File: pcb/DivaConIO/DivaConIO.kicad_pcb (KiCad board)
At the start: 2 copper layers, 65 x 75 mm, 59 parts, among them J1 Conn_01x06_MountingPin, J2 Conn_01x04_MountingPin, J3 Conn_01x06_MountingPin, J4 Conn_01x08_MountingPin, J5 JST_SH_BM03B-SRSS-TB, J6 Conn_01x05_MountingPin, J7 Conn_01x06_MountingPin, Q1 BSS138, Q2 BSS138, Q3 BSS138, Q4 BSS138, Q5 BSS138, SW1 SW_Push

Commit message: revision 1.0 pcb schematics and layout
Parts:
- removed C5, C6: 1u0, Capacitor_SMD:C_0603_1608Metric
- removed Q1: BSS138, Package_TO_SOT_SMD:SOT-23
- added C7: 100n, Capacitor_SMD:C_0603_1608Metric, F.Cu at (117.3, 124.9)
- added FID1: Fiducial, Fiducial:Fiducial_0.5mm_Mask1.5mm, F.Cu at (163.2, 142.0)
- added FID2: Fiducial, Fiducial:Fiducial_0.5mm_Mask1.5mm, F.Cu at (108.0, 76.8)
- added FID3: Fiducial, Fiducial:Fiducial_0.5mm_Mask1.5mm, F.Cu at (101.8, 83.0)
- added FID4: Fiducial, Fiducial:Fiducial_0.5mm_Mask1.5mm, F.Cu at (157.0, 148.2)
- added TP1: TestPoint, TestPoint:TestPoint_Pad_D2.0mm, F.Cu at (147.5, 87.8)
- added TP10: TestPoint, TestPoint:TestPoint_Pad_D2.0mm, F.Cu at (143.5, 135.5)
- added TP11: TestPoint, TestPoint:TestPoint_Pad_D2.0mm, F.Cu at (140.5, 142.8)
- added TP12: TestPoint, TestPoint:TestPoint_Pad_D2.0mm, F.Cu at (140.5, 138.7)
- added TP2: TestPoint, TestPoint:TestPoint_Pad_D2.0mm, F.Cu at (150.8, 79.2)
- added TP3: TestPoint, TestPoint:TestPoint_Pad_D2.0mm, F.Cu at (112.5, 135.5)
- added TP4: TestPoint, TestPoint:TestPoint_Pad_D2.0mm, F.Cu at (153.0, 82.5)
- added TP5: TestPoint, TestPoint:TestPoint_Pad_D2.0mm, F.Cu at (120.5, 133.0)
- added TP6: TestPoint, TestPoint:TestPoint_Pad_D2.0mm, F.Cu at (123.5, 133.0)
- added TP7: TestPoint, TestPoint:TestPoint_Pad_D2.0mm, F.Cu at (140.5, 130.0)
- added TP8: TestPoint, TestPoint:TestPoint_Pad_D2.0mm, F.Cu at (140.5, 133.0)
- added TP9: TestPoint, TestPoint:TestPoint_Pad_D2.0mm, F.Cu at (156.8, 112.5)
- added U1: 74HCT1G14, Package_TO_SOT_SMD:SC-74A-5_1.55x2.9mm_P0.95mm, F.Cu at (117.3, 121.8)
- J1, J3, J7: value Conn_01x06_MountingPin -> B6B-PH-SM4-TBT
- J2: value Conn_01x04_MountingPin -> B4B-PH-SM4-TBT
- J4: value Conn_01x08_MountingPin -> B8B-PH-SM4-TBT
- J5: value JST_SH_BM03B-SRSS-TB -> BM03B-SRSS-TBT
- R18: value 4K7 -> 330R
- R19: value 10R -> 10K
- SW1: footprint Button_Switch_SMD:SW_Push_SPST_NO_Alps_SKRK -> DivaConIO:SW_Push_SPST_NO_Alps_SKRP
- moved SYM2 37.6 mm to (129.0, 101.0)
- moved SYM1 37.5 mm to (136.0, 100.5)
- moved R16 24.3 mm to (146.5, 125.4), turned to 90 degrees
- moved R17 23.8 mm to (146.5, 122.3), turned to -90 degrees
- moved R9 23.7 mm to (117.3, 102.2), turned to 0 degrees
- moved R10 23.2 mm to (117.3, 104.8), turned to 0 degrees
- moved R32 20.3 mm to (147.2, 109.9), turned to 180 degrees
- moved R11 20.2 mm to (117.3, 109.9), turned to 0 degrees
- moved R31 19.8 mm to (147.2, 112.4), turned to 180 degrees
- moved R12 19.7 mm to (117.3, 112.4), turned to 0 degrees
- moved R30 19.3 mm to (147.2, 114.9), turned to 180 degrees
- moved R29 18.8 mm to (147.2, 117.5), turned to 180 degrees
- moved R14 18.7 mm to (117.3, 115.5), turned to 0 degrees
- moved R6 18.3 mm to (117.3, 92.3), turned to 0 degrees
- moved R18 16.8 mm to (114.7, 123.8), turned to -90 degrees
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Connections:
- net /LED_Circle renamed /LED-_Circle
- net /LED_Cross renamed /LED-_Cross
- net /LED_Square renamed /LED-_Square
- net /LED_Triangle renamed /LED-_Triangle
- J4 pad 4: Net-(J4-Pin_4) -> /Slider_I2C1_SDA
- J4 pad 6: /Slider_I2C1_SDA -> Net-(J4-Pin_6)
- J5 pad 1: Net-(A1-SWDIO) -> Net-(A1-SWCLK)
- J5 pad 3: Net-(A1-SWCLK) -> Net-(A1-SWDIO)
- R13 pad 2: /Slider_I2C1_SDA -> /Slider_I2C1_SCL
- R15 pad 2: /Slider_I2C1_SCL -> /Slider_I2C1_SDA
- R18 pad 1: +5V -> Net-(R18-Pad1)
- R18 pad 2: Net-(J4-Pin_4) -> Net-(J4-Pin_6)
- R19 pad 2: Net-(Q1-G) -> GND
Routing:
- net GND: track 123.4 -> 25.3 mm, vias 16 -> 512
- net +5V: track 139.6 -> 187.6 mm, vias 4 -> 25
- net +3V3: track 199.6 -> 245.4 mm, vias 24 -> 39
- net Net-(J4-Pin_6): track 0.00 -> 27.0 mm
- net /Slider_LED_Data: track 22.6 -> 7.62 mm
- net /Display_I2C0_SDA: track 33.3 -> 46.5 mm
- net Net-(J4-Pin_4): track 9.00 -> 0.00 mm
- net /Display_I2C0_SCL: track 40.7 -> 48.7 mm
- net Net-(A1-SWDIO): track 30.2 -> 36.7 mm, vias 0 -> 2
- net /LED-_Triangle: track 10.1 -> 16.5 mm
- net /Slider_I2C1_SCL: track 21.9 -> 27.8 mm
- net /Button_L1: track 32.2 -> 37.9 mm
- net /Button_R3: track 22.4 -> 27.9 mm
- net Net-(A1-SWCLK): track 31.5 -> 36.6 mm
- net /Button_Right: track 25.4 -> 30.4 mm
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- added copper zone on B.Cu, net +3V3
- added copper zone on F.Cu, net +3V3
- added copper zone on B.Cu, net +5V
- added copper zone on F.Cu, net +5V
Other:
- outline, holes or cut-outs redrawn
- board text added: "${TITLE} ${COMPANY} Rev ${REVISION} ${ISSUE_DATE}"
- board text added: "0.2032 mm / 0.2032 mm"
- board text added: "0.4000 mm"
- board text added: "1"
- board text added: "1.6000 mm"
- board text added: "2"
- board text added: "3V3"
- board text added: "5V"
- board text added: "65.0000 mm x 75.0000 mm"
- board text added: "BOARD CHARACTERISTICS"
- board text added: "Board Thickness:"
- board text added: "Board overall dimensions:"
- board text added: "Castellated pads:"
- board text added: "Copper Finish:"
- board text added: "Copper Layer Count:"
- board text added: "ENIG"
- board text added: "Edge card connectors:"
- board text added: "GND"
- board text added: "Impedance Control:"
- board text added: "LED_DATA"
- board text added: "Min hole diameter:"
- board text added: "Min track/spacing:"
- board text added: "No"
- board text added: "Plated Board Edge:"
- board text added: "RESET"
- board text added: "SCL0"
- board text added: "SCL1"
- board text added: "SDA0"
- board text added: "SDA1"
- board text added: "SN:"
- board text added: "SWCLK"
- board text added: "SWDIO"
- board text added: "nRST"

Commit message: revision 1.1 pcb schematics and layout
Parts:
- removed the R23 at (146.5, 95.8)
- removed the R26 at (152.2, 99.4)
- added R20: 10R, Resistor_SMD:R_0603_1608Metric, F.Cu at (147.2, 95.9)
- added R32: 330R, Resistor_SMD:R_0603_1608Metric, F.Cu at (153.3, 104.5)
- moved TP6 56.8 mm to (151.3, 83.5), turned to 0 degrees
- moved TP5 54.9 mm to (151.3, 87.5), turned to 0 degrees
- moved TP3 54.2 mm to (158.0, 106.0)
- moved TP2 53.1 mm to (135.0, 130.0)
- moved SYM1 51.2 mm to (106.0, 142.0)
- moved SYM2 47.8 mm to (145.0, 146.0)
- moved TP1 45.7 mm to (130.0, 130.0)
- moved J6 41.7 mm to (160.0, 128.0), turned to -90 degrees
- moved R31 35.4 mm to (149.0, 109.6), turned to -90 degrees
- moved TP11 34.9 mm to (151.3, 109.6), turned to 0 degrees
- moved R11 33.4 mm to (115.7, 123.4), turned to 90 degrees
- moved C5 31.6 mm to (148.1, 131.7)
- moved R23 31.5 mm to (148.1, 125.1), turned to 0 degrees
- moved U1 31.5 mm to (148.1, 128.4)
- moved R26 31.3 mm to (145.2, 130.9)
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- renumbered C7 to C5, FID3 to FID2, FID2 to FID3, J6 to J4, J4 to J6, Q5 to Q1, Q4 to Q2, Q2 to Q4, R9 to R10, R31 to R11, R10 to R12, R30 to R13, R11 to R14, R29 to R15, R12 to R16, R14 to R17, R20 to R18, R24 to R19, R19 to R23, R28 to R24, R18 to R26, R17 to R28, R16 to R29, R15 to R30, R13 to R31, R32 to R9
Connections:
- A1 pad 17: /Slider_LED_Data -> /Button_Circle
- A1 pad 19: /Slider_I2C1_SDA -> /Button_Cross
- A1 pad 20: /Slider_I2C1_SCL -> /Button_Square
- A1 pad 21: /Display_I2C0_SDA -> /Button_Triangle
- A1 pad 22: /Display_I2C0_SCL -> /Slider_LED_Data
- A1 pad 24: /Button_Triangle -> /Slider_I2C1_SDA
- A1 pad 25: /Button_Square -> /Slider_I2C1_SCL
- A1 pad 26: /Button_Cross -> /Display_I2C0_SDA
- A1 pad 27: /Button_Circle -> /Display_I2C0_SCL
- A1 pad 29: /LED_En_Triangle -> /LED_En_Circle
- A1 pad 31: /LED_En_Square -> /LED_En_Cross
- A1 pad 32: /LED_En_Cross -> /LED_En_Square
- A1 pad 34: /LED_En_Circle -> /LED_En_Triangle
- J4 pad 2: /Button_Circle -> /Button_Triangle
- J4 pad 3: /Button_Cross -> /Button_Square
- J4 pad 4: /Button_Square -> /Button_Cross
- J4 pad 5: /Button_Triangle -> /Button_Circle
- J6 pad 1: GND -> /Display_I2C0_SCL
- J6 pad 2: /Display_I2C0_SCL -> /Display_I2C0_SDA
- J6 pad 3: /Display_I2C0_SDA -> /Slider_I2C1_SCL
- J6 pad 5: /Slider_I2C1_SCL -> +3V3
- J6 pad 6: Net-(J4-Pin_6) -> GND
- J6 pad 7: +3V3 -> +5V
- J6 pad 8: +5V -> Net-(J6-Pin_8)
- J7 pad 1: /LED-_Circle -> +5V
- J7 pad 2: /LED-_Cross -> +5V
- J7 pad 3: /LED-_Square -> /LED-_Triangle
- J7 pad 4: /LED-_Triangle -> /LED-_Square
- J7 pad 5: +5V -> /LED-_Cross
- J7 pad 6: +5V -> /LED-_Circle
- Q2 pad 3: Net-(Q4-D) -> Net-(Q2-D)
- Q4 pad 1: Net-(Q2-G) (its old number) -> Net-(Q4-G)
- Q4 pad 3: Net-(Q2-D) -> Net-(Q4-D)
- R19 pad 1: /LED_En_Circle -> /LED_En_Triangle
- R21 pad 1: /LED_En_Triangle -> /LED_En_Cross
- R21 pad 2: Net-(Q2-G) (its old number) -> Net-(Q3-G)
- R22 pad 1: /LED_En_Square -> /LED_En_Circle
- R22 pad 2: Net-(Q3-G) -> Net-(Q4-G)
- R24 pad 1: /LED-_Circle -> /LED-_Triangle
- R25 pad 1: /LED-_Triangle -> /LED-_Square
- R26 pad 2: Net-(J4-Pin_6) -> Net-(J6-Pin_8)
- R27 pad 2: Net-(Q4-D) -> Net-(Q3-D)
- R28 pad 2: /Display_I2C0_SCL -> /Slider_I2C1_SDA
- R29 pad 2: /Display_I2C0_SDA -> /Slider_I2C1_SCL
- R30 pad 2: /Slider_I2C1_SDA -> /Display_I2C0_SDA
- R31 pad 2: /Slider_I2C1_SCL -> /Display_I2C0_SCL
- TP1 pad 1: +3V3 -> Net-(A1-SWCLK)
- TP10 pad 1: GND -> /Display_I2C0_SDA
- TP11 pad 1: Net-(A1-SWCLK) -> /Display_I2C0_SCL
- TP12 pad 1: Net-(A1-SWDIO) -> GND
- TP2 pad 1: +5V -> Net-(A1-SWDIO)
- TP3 pad 1: Net-(J4-Pin_6) -> Net-(A1-RUN)
- TP4 pad 1: GND -> +5V
- TP5 pad 1: /Slider_I2C1_SCL -> +3V3
- TP6 pad 1: /Slider_I2C1_SDA -> GND
- TP7 pad 1: /Display_I2C0_SDA -> Net-(J6-Pin_8)
- TP8 pad 1: /Display_I2C0_SCL -> /Slider_I2C1_SDA
- TP9 pad 1: Net-(A1-RUN) -> /Slider_I2C1_SCL
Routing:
- net GND: track 25.3 -> 270.6 mm, vias 512 -> 176
- net +5V: track 187.6 -> 134.0 mm, vias 25 -> 0
- net +3V3: track 245.4 -> 289.1 mm, vias 39 -> 0
- net Net-(J4-Pin_6): track 27.0 -> 0.00 mm
- net Net-(A1-SWDIO): track 36.7 -> 12.6 mm, vias 2 -> 0
- net Net-(A1-SWCLK): track 36.6 -> 12.6 mm
- net /Display_I2C0_SCL: track 48.7 -> 29.9 mm, vias 2 -> 0
- net Net-(J6-Pin_8): track 0.00 -> 17.5 mm
- net /Display_I2C0_SDA: track 46.5 -> 29.8 mm, vias 2 -> 0
- net Net-(A1-VBUS): track 4.64 -> 15.1 mm
- net /LED-_Triangle: track 16.5 -> 7.18 mm
- net /Button_Triangle: track 31.0 -> 22.6 mm
- net /Button_Circle: track 35.5 -> 42.5 mm
- net Net-(A1-RUN): track 33.9 -> 27.4 mm
- net /LED-_Square: track 12.1 -> 6.79 mm
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- removed copper zone on B.Cu, net +3V3
- removed copper zone on B.Cu, net +5V
- removed copper zone on F.Cu, net +5V

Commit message: generate revision 1.1 gerber files
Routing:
- net GND: track 270.6 -> 270.0 mm
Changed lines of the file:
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@@
 	(segment
 		(start 124.892 116.218)
-		(end 128.956 112.154)
+		(end 130.988 110.122)
 		(width 0.254)
 		(layer "F.Cu")
@@
 	)
 	(segment
-		(start 130.988 110.122)
-		(end 128.956 112.154)
-		(width 0.254)
-		(layer "F.Cu")
-		(net 2)
-	)
-	(segment
 		(start 135.56 114.313032)
 		(end 135.56 111.9)
@@
 	)
 	(segment
-		(start 164.099 92)
-		(end 164.099 130)
-		(width 0.8)
-		(layer "F.Cu")
-		(net 4)
-	)
-	(segment
 		(start 155.88 90)
 		(end 155.88 91.58)
@@
 	)
 	(segment
-		(start 164.099 130)
+		(start 164.099 92)
 		(end 164.099 132.22)
 		(width 0.8)
@@
 	)
 	(segment
-		(start 147.119 127.26)
-		(end 147.119 127.869)
-		(width 0.254)
-		(layer "F.Cu")
-		(net 32)
-	)
-	(segment
 		(start 144.704 94.12)
 		(end 144.704 94.628)
@@
 		(width 0.254)
 		(layer "F.Cu")
-		(net 49)
-	)
-	(segment
-		(start 145.25 131.813)
-		(end 145.212 131.775)
-		(width 0.254)
-		(layer "F.Cu")

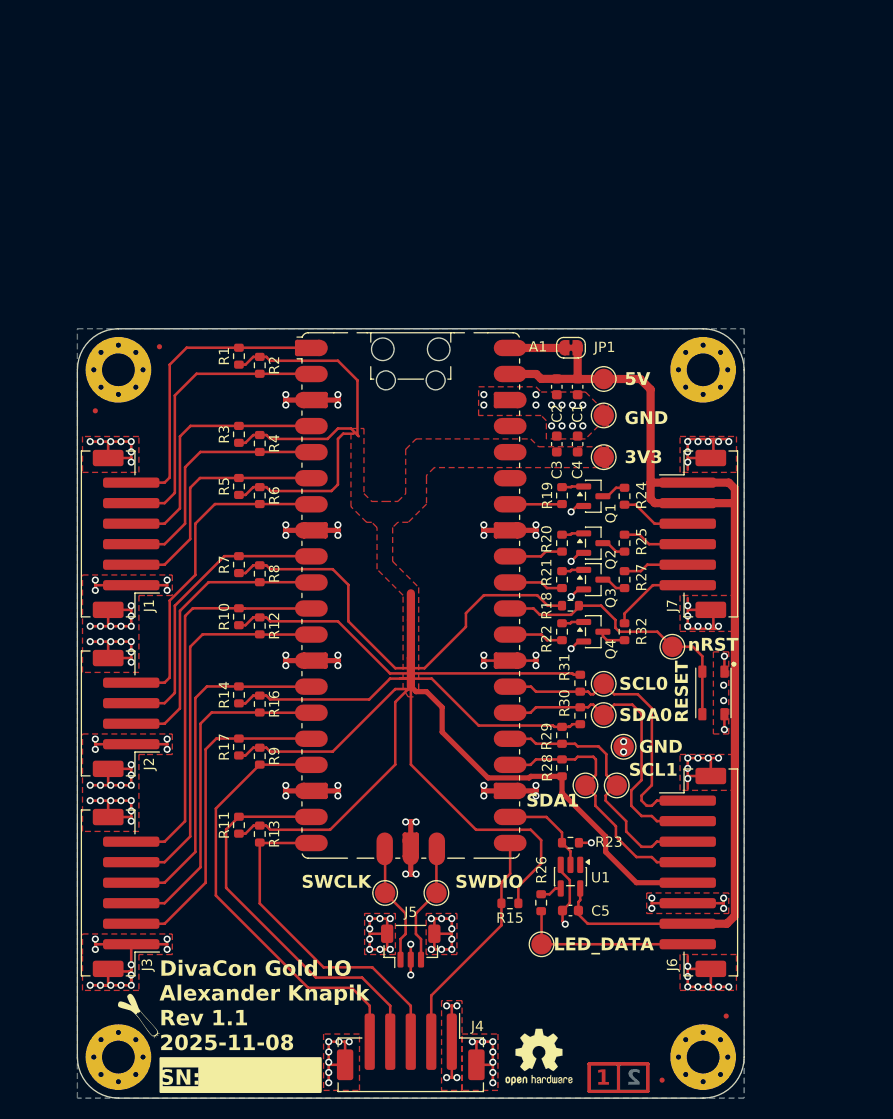
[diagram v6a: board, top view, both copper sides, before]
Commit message: Update PCBs to purchased revision
Main edit is using a ULN2003 NPN transistor array over discrete MOSFETs.
This was chosen because there was limited board space to put in
pull-down resistors on the board and it was complicating the single
layer routing. The PCB had to be expanded to 70x75mm anyways to
accommodate the SOIC ic anyways.

The schematics of the IO board were also updated to use net labels over
direct wiring. Due to the JST connectors and the Pi Pico schematic
symbol being mirrored, it was getting too difficult to have an
understandable schematic.

Minor edit was changing LED_DATA to nLED_DATA to signify that it is
an active low signal.
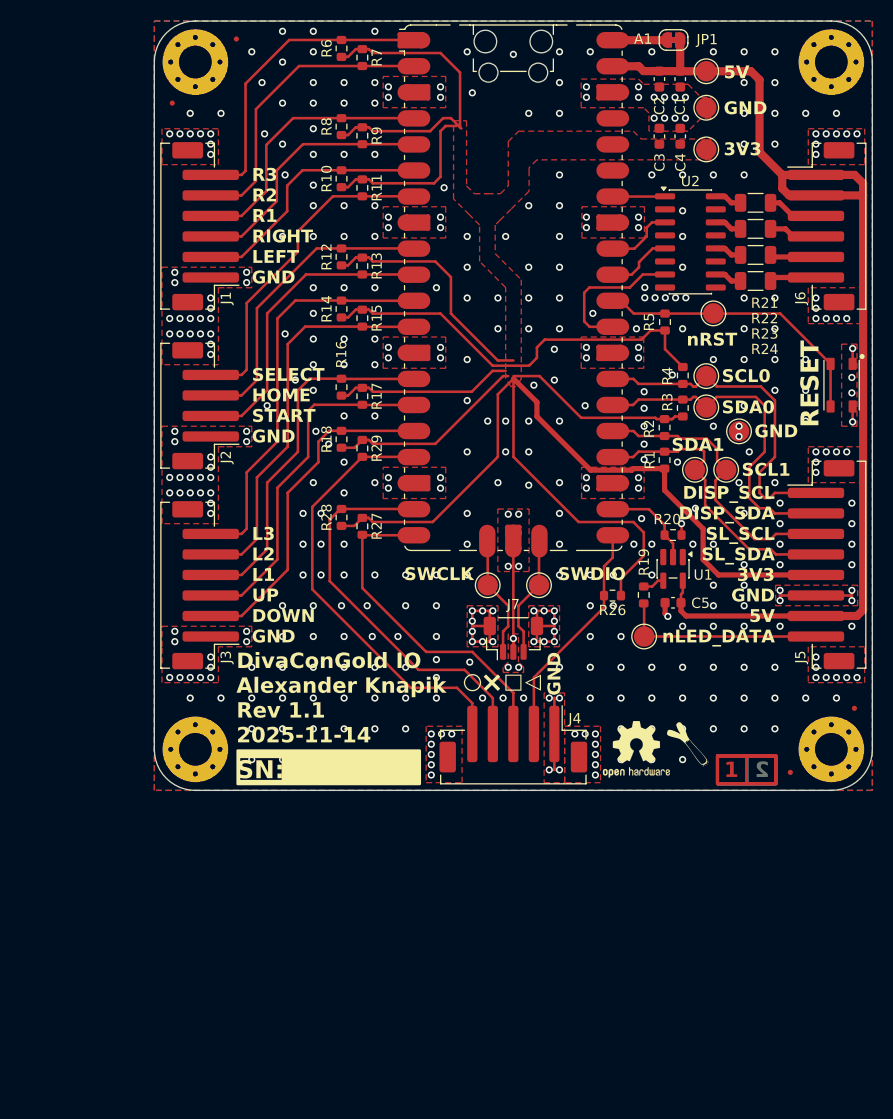
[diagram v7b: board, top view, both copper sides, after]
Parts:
- removed Q1, Q2, Q3, Q4: BSS138, Package_TO_SOT_SMD:SOT-23
- removed the R19 at (147.2, 91.3)
- removed the R20 at (147.2, 95.9)
- removed R25, R32: 330R, Resistor_SMD:R_0603_1608Metric
- removed the R27 at (153.3, 99.5)
- added R23: 270R, Resistor_SMD:R_1206_3216Metric, F.Cu at (166.1, 67.8)
- added U2: ULN2003D1013TR, Package_SO:SOIC-16_3.9x9.9mm_P1.27mm, F.Cu at (159.8, 66.5)
- H1, H2, H3, H4: value MountingHole_Pad -> Standoff_M3
- J4: value Conn_01x05_MountingPin -> B5B-PH-SM4-TBT
- R19: renamed from R26; value 330R -> 470R
- R21, R22: value 10R -> 270R; footprint Resistor_SMD:R_0603_1608Metric -> Resistor_SMD:R_1206_3216Metric
- R24: value 330R -> 270R; footprint Resistor_SMD:R_0603_1608Metric -> Resistor_SMD:R_1206_3216Metric
- SW1: value SW_Push -> SKRPABE010
- U1: value 74HCT1G14 -> 74HCT1G14GV,125
- moved SYM1 59.7 mm to (159.5, 115.5)
- moved R22 43.6 mm to (166.1, 65.3), turned to 0 degrees
- moved R21 41.3 mm to (166.1, 62.7), turned to 0 degrees
- moved TP10 32.7 mm to (162.0, 73.5)
- moved TP11 32.7 mm to (164.5, 85.0)
- moved TP6 32.6 mm to (163.2, 88.8)
- moved TP8 32.6 mm to (160.2, 88.8)
- moved FID1 32.5 mm to (175.8, 112.0)
- moved FID4 32.5 mm to (169.5, 118.2)
- moved H1 32.5 mm to (173.5, 49.0)
- moved H3 32.5 mm to (173.5, 116.0)
- moved J5 32.5 mm to (172.5, 98.0)
- moved J6 32.5 mm to (172.5, 65.0)
- moved SW1 32.5 mm to (174.5, 80.5)
- moved C3 31.6 mm to (156.7, 56.2)
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- renumbered FID3 to FID2, FID2 to FID3, J6 to J5, J7 to J6, J5 to J7, R28 to R1, R5 to R10, R6 to R11, R7 to R12, R8 to R13, R10 to R14, R12 to R15, R14 to R16, R16 to R17, R17 to R18, R29 to R2, R23 to R20, R15 to R26, R13 to R27, R11 to R28, R9 to R29, R30 to R3, R31 to R4, R18 to R5, R1 to R6, R2 to R7, R3 to R8, R4 to R9, TP3 to TP10, TP12 to TP11, TP6 to TP12, TP4 to TP3, TP5 to TP4, TP7 to TP5, TP9 to TP6, TP11 to TP7, TP10 to TP9
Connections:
- net Net-(J6-Pin_8) renamed /nSlider_LED_Data
- A1 pad 1: /Button_Left -> /Button_R3
- A1 pad 10: /Button_Home -> /Button_Start
- A1 pad 11: /Button_Down -> /Button_L3
- A1 pad 12: /Button_Up -> /Button_L2
- A1 pad 15: /Button_L2 -> /Button_Up
- A1 pad 16: /Button_L3 -> /Button_Down
- A1 pad 2: /Button_Right -> /Button_R2
- A1 pad 4: /Button_R3 -> /Button_R1
- A1 pad 5: /Button_R2 -> /Button_Right
- A1 pad 6: /Button_R1 -> /Button_Left
- A1 pad 9: /Button_Start -> /Button_Home
- J1 pad 2: /Button_R1 -> /Button_Left
- J1 pad 3: /Button_R2 -> /Button_Right
- J1 pad 4: /Button_R3 -> /Button_R1
- J1 pad 5: /Button_Right -> /Button_R2
- J1 pad 6: /Button_Left -> /Button_R3
- J2 pad 2: /Button_Home -> /Button_Start
- J2 pad 3: /Button_Start -> /Button_Home
- J3 pad 2: /Button_L3 -> /Button_Down
- J3 pad 3: /Button_L2 -> /Button_Up
- J3 pad 5: /Button_Up -> /Button_L2
- J3 pad 6: /Button_Down -> /Button_L3
- R10 pad 2: /Button_R1 -> /Button_Left
- R12 pad 2: /Button_Start -> /Button_Home
- R13 pad 2: /Button_Home -> /Button_Start
- R14 pad 2: /Button_Down -> /Button_L3
- R15 pad 2: /Button_Up -> /Button_L2
- R17 pad 2: /Button_L2 -> /Button_Up
- R18 pad 2: /Button_L3 -> /Button_Down
- R21 pad 1: /LED_En_Cross -> Net-(U2-O1)
- R21 pad 2: Net-(Q3-G) -> /LED-_Triangle
- R22 pad 1: /LED_En_Circle -> Net-(U2-O3)
- R22 pad 2: Net-(Q4-G) -> /LED-_Square
- R24 pad 1: /LED-_Triangle -> Net-(U2-O7)
- R24 pad 2: Net-(Q1-D) -> /LED-_Circle
- R6 pad 2: /Button_Left -> /Button_R3
- R7 pad 2: /Button_Right -> /Button_R2
- R8 pad 2: /Button_R3 -> /Button_R1
- R9 pad 2: /Button_R2 -> /Button_Right
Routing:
- net GND: track 270.0 -> 60.0 mm, vias 176 -> 439
- net +3V3: track 289.1 -> 262.6 mm
- net +5V: track 134.0 -> 110.1 mm
- net /LED_En_Circle: track 5.28 -> 14.4 mm
- net /Button_Down: track 38.7 -> 30.6 mm
- net /Button_Up: track 37.6 -> 32.0 mm
- net /Button_Right: track 28.3 -> 23.0 mm
- net /Button_Left: track 29.4 -> 24.8 mm
- net /Button_L3: track 32.6 -> 37.2 mm
- net /LED-_Triangle: track 7.18 -> 2.69 mm
- net /LED-_Square: track 6.79 -> 2.50 mm
- net /LED-_Circle: track 8.50 -> 4.57 mm
- net /Display_I2C0_SDA: track 29.8 -> 33.1 mm
- net /Display_I2C0_SCL: track 29.9 -> 33.1 mm
- net Net-(Q4-D): track 2.70 -> 0.00 mm
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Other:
- board size 65 x 75 mm -> 70 x 75 mm
- board text added: "5V LED+"
- board text added: "5V VCC"
- board text added: "70.0000 mm x 75.0000 mm"
- board text added: "DISPLAY SCL0"
- board text added: "DISPLAY SDA0"
- board text added: "DISP_SCL"
- board text added: "DISP_SDA"
- board text added: "DOWN"
- board text added: "HAL lead-free"
- board text added: "HOME"
- board text added: "L1"
- board text added: "L2"
- board text added: "L3"
- board text added: "LED-"
- board text added: "LEFT"
- board text added: "R1"
- board text added: "R2"
- board text added: "R3"
- board text added: "RIGHT"
- board text added: "SELECT"
- board text added: "SLIDER SCL1"
- board text added: "SLIDER SDA1"
- board text added: "SL_SCL"
- board text added: "SL_SDA"
- board text added: "START"
- board text added: "UP"
- board text added: "nLED DATA"
- board text added: "nLED_DATA"
- board text added: "×"
- board text added: "□"
- board text added: "△"
- board text added: "○"
- board text removed: "65.0000 mm x 75.0000 mm"
- board text removed: "ENIG"
- board text removed: "LED_DATA"
